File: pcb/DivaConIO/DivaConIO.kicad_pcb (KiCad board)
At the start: 2 copper layers, 55.9 x 70.5 mm, 35 parts, among them J1 DPad Buttons, J10 SWD, J2 Slider i2c, J3 Display i2c, J4 Face Buttons, J5 Button LEDs, J6 L Buttons, J7 Fn Buttons, J8 R Buttons, J9 Slider LEDs, Q1 BC847, Q2 BC847, Q3 BC847, Q4 BC847, SW1 Reset, U1 Pico, U2 SN74LVC1T45DCK

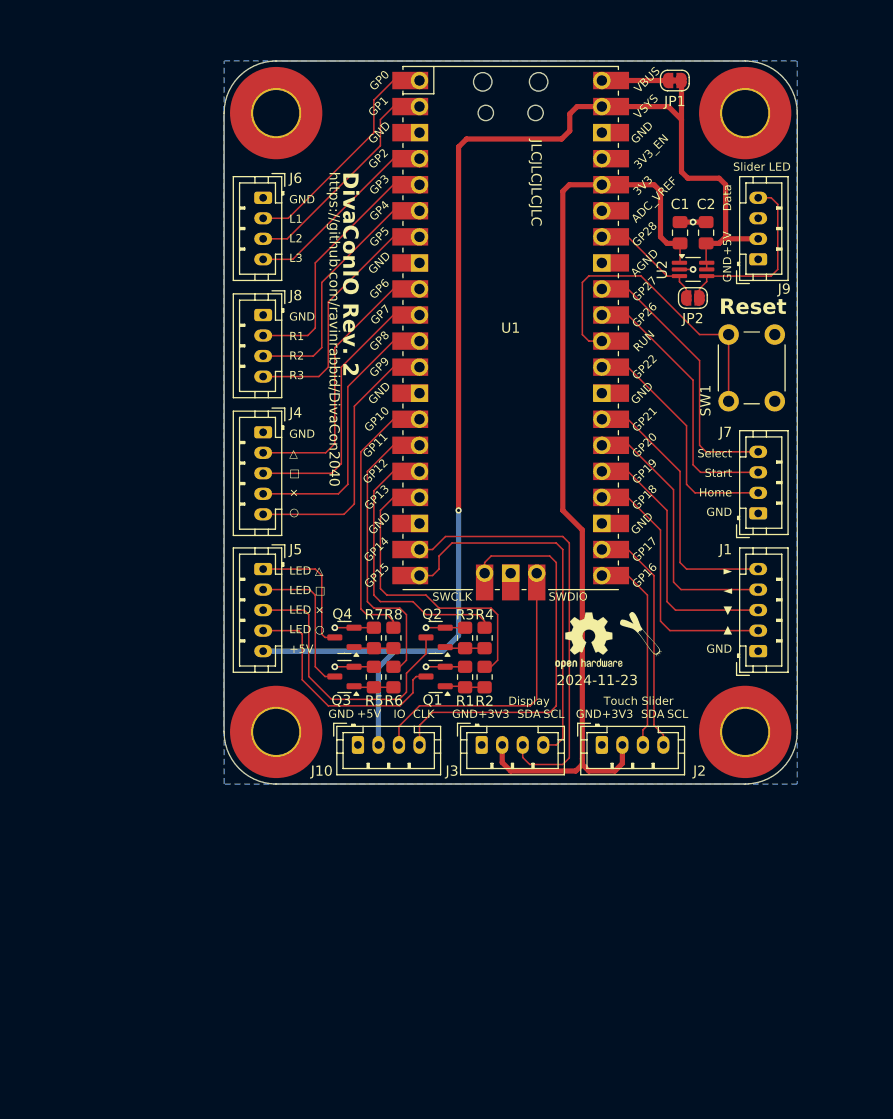
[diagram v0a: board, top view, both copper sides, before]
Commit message: relaid out IO board
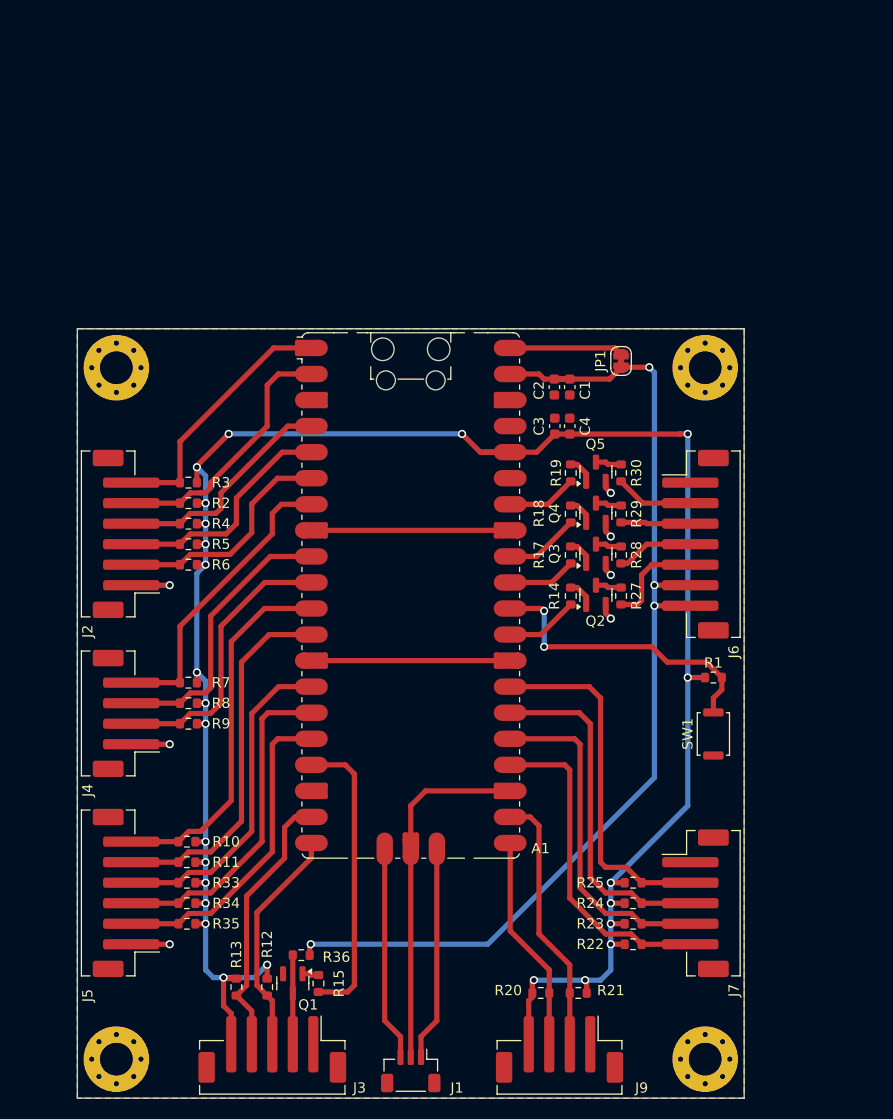
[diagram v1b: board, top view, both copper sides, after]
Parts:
- removed J10: SWD, Connector_JST:JST_PH_B4B-PH-K_1x04_P2.00mm_Vertical
- removed J8: R Buttons, Connector_JST:JST_PH_B4B-PH-K_1x04_P2.00mm_Vertical
- removed JP2: Bridge LED Data, Jumper:SolderJumper-2_P1.3mm_Open_RoundedPad1.0x1.5mm
- removed REF**: OSHW-Logo2_7.3x6mm_SilkScreen, Symbol:OSHW-Logo2_7.3x6mm_SilkScreen
- removed REF**: LOGO, CustomLogos:Leek-Logo_6.3mm_Silkscreen
- removed U1: Pico, DivaConIO:RPi_Pico_SMD_TH
- removed U2: SN74LVC1T45DCK, Package_TO_SOT_SMD:SOT-363_SC-70-6_Handsoldering
- added A1: RaspberryPi_Pico, Module:RaspberryPi_Pico_SMD_HandSolder, F.Cu at (132.5, 101.0)
- added C3: 1u0, Capacitor_SMD:C_0603_1608Metric, F.Cu at (146.5, 84.5)
- added C4: 100n, Capacitor_SMD:C_0603_1608Metric, F.Cu at (148.0, 84.5)
- added Q5: BSS138, Package_TO_SOT_SMD:SOT-23, F.Cu at (150.6, 88.9)
- added R10: 10K, Resistor_SMD:R_0603_1608Metric, F.Cu at (110.7, 125.0)
- added R11: 10K, Resistor_SMD:R_0603_1608Metric, F.Cu at (110.7, 127.0)
- added R12: 4K7, Resistor_SMD:R_0603_1608Metric, F.Cu at (118.5, 139.2)
- added R13: 4K7, Resistor_SMD:R_0603_1608Metric, F.Cu at (115.5, 139.2)
- added R14: 10R, Resistor_SMD:R_0603_1608Metric, F.Cu at (148.1, 101.0)
- added R15: 10R, Resistor_SMD:R_0603_1608Metric, F.Cu at (123.5, 138.8)
- added R17: 10R, Resistor_SMD:R_0603_1608Metric, F.Cu at (148.1, 97.0)
- added R18: 10R, Resistor_SMD:R_0603_1608Metric, F.Cu at (148.1, 93.0)
- added R19: 10R, Resistor_SMD:R_0603_1608Metric, F.Cu at (148.1, 89.0)
- added R20: 4K7, Resistor_SMD:R_0603_1608Metric, F.Cu at (145.2, 139.8)
- added R21: 4K7, Resistor_SMD:R_0603_1608Metric, F.Cu at (148.8, 139.8)
- added R22: 10K, Resistor_SMD:R_0603_1608Metric, F.Cu at (154.2, 135.0)
- added R23: 10K, Resistor_SMD:R_0603_1608Metric, F.Cu at (154.2, 133.0)
- added R24: 10K, Resistor_SMD:R_0603_1608Metric, F.Cu at (154.2, 131.0)
- added R25: 10K, Resistor_SMD:R_0603_1608Metric, F.Cu at (154.2, 129.0)
- added R27: 330R, Resistor_SMD:R_0603_1608Metric, F.Cu at (153.0, 101.0)
- added R28: 330R, Resistor_SMD:R_0603_1608Metric, F.Cu at (153.0, 97.0)
- added R29: 330R, Resistor_SMD:R_0603_1608Metric, F.Cu at (153.0, 93.0)
- added R30: 330R, Resistor_SMD:R_0603_1608Metric, F.Cu at (153.0, 89.0)
- added R33: 10K, Resistor_SMD:R_0603_1608Metric, F.Cu at (110.7, 129.0)
- added R34: 10K, Resistor_SMD:R_0603_1608Metric, F.Cu at (110.7, 131.0)
- added R35: 10K, Resistor_SMD:R_0603_1608Metric, F.Cu at (110.7, 133.0)
- added R36: 4K7, Resistor_SMD:R_0603_1608Metric, F.Cu at (121.8, 136.1)
- added R9: 10K, Resistor_SMD:R_0603_1608Metric, F.Cu at (110.8, 113.5)
- C1: value 0.1uF -> 1u0; footprint Capacitor_SMD:C_0805_2012Metric_Pad1.18x1.45mm_HandSolder -> Capacitor_SMD:C_0603_1608Metric
- C2: value 0.1uF -> 100n; footprint Capacitor_SMD:C_0805_2012Metric_Pad1.18x1.45mm_HandSolder -> Capacitor_SMD:C_0603_1608Metric
- H1, H2, H3, H4: footprint MountingHole:MountingHole_4.5mm_Pad_TopOnly -> MountingHole:MountingHole_3.2mm_M3_Pad_Via
- J1: value DPad Buttons -> JST_SH_BM03B-SRSS-TB; footprint Connector_JST:JST_PH_B5B-PH-K_1x05_P2.00mm_Vertical -> Connector_JST:JST_SH_BM03B-SRSS-TB_1x03-1MP_P1.00mm_Vertical
- J2: value Slider i2c -> Conn_01x06; footprint Connector_JST:JST_PH_B4B-PH-K_1x04_P2.00mm_Vertical -> Connector_JST:JST_PH_B6B-PH-SM4-TB_1x06-1MP_P2.00mm_Vertical
- J3: value Display i2c -> Conn_01x05; footprint Connector_JST:JST_PH_B4B-PH-K_1x04_P2.00mm_Vertical -> Connector_JST:JST_PH_B5B-PH-SM4-TB_1x05-1MP_P2.00mm_Vertical
- J4: value Face Buttons -> Fn Buttons; footprint Connector_JST:JST_PH_B5B-PH-K_1x05_P2.00mm_Vertical -> Connector_JST:JST_PH_B4B-PH-SM4-TB_1x04-1MP_P2.00mm_Vertical
- J5: value Button LEDs -> Conn_01x06; footprint Connector_JST:JST_PH_B5B-PH-K_1x05_P2.00mm_Vertical -> Connector_JST:JST_PH_B6B-PH-SM4-TB_1x06-1MP_P2.00mm_Vertical
- J6: value L Buttons -> Conn_01x07; footprint Connector_JST:JST_PH_B4B-PH-K_1x04_P2.00mm_Vertical -> Connector_JST:JST_PH_B7B-PH-SM4-TB_1x07-1MP_P2.00mm_Vertical
- J7: value Fn Buttons -> Conn_01x05; footprint Connector_JST:JST_PH_B4B-PH-K_1x04_P2.00mm_Vertical -> Connector_JST:JST_PH_B5B-PH-SM4-TB_1x05-1MP_P2.00mm_Vertical
- J9: value Slider LEDs -> Display i2c; footprint Connector_JST:JST_PH_B4B-PH-K_1x04_P2.00mm_Vertical -> Connector_JST:JST_PH_B4B-PH-SM4-TB_1x04-1MP_P2.00mm_Vertical
- JP1: value Bridge VSYS -> SolderJumper_2_Bridged
- Q1, Q2, Q3, Q4: value BC847 -> BSS138
- R1, R2, R3, R4, R5, R6, R7, R8: value 4.7k -> 10K; footprint Resistor_SMD:R_0805_2012Metric_Pad1.20x1.40mm_HandSolder -> Resistor_SMD:R_0603_1608Metric
- SW1: value Reset -> SW_Push; footprint Button_Switch_THT:SW_PUSH_6mm -> Button_Switch_SMD:SW_Push_SPST_NO_Alps_SKRK
- moved H2 110.7 mm to (103.8, 146.2)
- moved J9 79.4 mm to (147.0, 145.2), turned to 180 degrees
- moved J6 54.0 mm to (160.2, 96.0)
- moved J1 53.1 mm to (132.5, 147.3), turned to 180 degrees
- moved J2 50.7 mm to (104.8, 95.0), turned to 90 degrees
- moved H1 48.6 mm to (161.2, 78.8)
- moved H4 38.8 mm to (103.8, 78.8)
- moved J7 38.5 mm to (160.2, 131.0), turned to -90 degrees
- moved J3 36.0 mm to (119.0, 145.2), turned to 180 degrees
- moved R2 34.5 mm to (110.8, 90.0), turned to 180 degrees
- moved J5 34.3 mm to (104.8, 130.0), turned to 90 degrees
- moved Q1 33.0 mm to (121.0, 138.8), turned to -90 degrees
- moved SW1 32.5 mm to (162.0, 114.5)
- moved H3 32.1 mm to (161.2, 146.2)
- moved R4 30.9 mm to (110.8, 94.0), turned to 180 degrees
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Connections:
- C1 pad 1: +3V3 -> +5V
- J1 pad 1: GND -> Net-(A1-SWDIO)
- J1 pad 2: Button Up -> GND
- J1 pad 3: Button Down -> Net-(A1-SWCLK)
- J2 pad 2: +3V3 -> /Button_R1
- J2 pad 3: Slider SDA -> /Button_R2
- J2 pad 4: Slider SCL -> /Button_R3
- J3 pad 2: +3V3 -> Net-(J3-Pin_2)
- J3 pad 3: Display SDA -> /Slider_I2C1_SCL
- J3 pad 4: Display SCL -> /Slider_I2C1_SDA
- J4 pad 2: Button Triangle -> /Button_Home
- J4 pad 3: Button Square -> /Button_Start
- J4 pad 4: Button Cross -> /Button_Select
- J5 pad 1: Net-(J5-Pin_1) -> GND
- J5 pad 2: Net-(J5-Pin_2) -> /Button_L3
- J5 pad 3: Net-(J5-Pin_3) -> /Button_L2
- J5 pad 4: Net-(J5-Pin_4) -> /Button_L1
- J5 pad 5: +5V -> /Button_Up
- J6 pad 2: Button L1 -> /LED_Circle
- J6 pad 3: Button L2 -> /LED_Cross
- J6 pad 4: Button L3 -> /LED_Square
- J7 pad 2: Button Home -> /Button_Circle
- J7 pad 3: Button Start -> /Button_Cross
- J7 pad 4: Button Select -> /Button_Square
- J9 pad 2: +5V -> /Display_I2C0_SCL
- J9 pad 3: unconnected-(J9-Pin_3-Pad3) -> /Display_I2C0_SDA
- J9 pad 4: Net-(J9-Pin_4) -> +3V3
- Q1 pad 1: Net-(Q1-B) -> Net-(Q1-G)
- Q1 pad 3: Net-(J5-Pin_4) -> Net-(J3-Pin_2)
- Q2 pad 1: Net-(Q2-B) -> Net-(Q2-G)
- Q2 pad 3: Net-(J5-Pin_3) -> Net-(Q2-D)
- Q3 pad 1: Net-(Q3-B) -> Net-(Q3-G)
- Q3 pad 3: Net-(J5-Pin_2) -> Net-(Q3-D)
- Q4 pad 1: Net-(Q4-B) -> Net-(Q4-G)
- Q4 pad 3: Net-(J5-Pin_1) -> Net-(Q4-D)
- R1 pad 1: GND -> +3V3
- R1 pad 2: Net-(Q1-B) -> Net-(A1-RUN)
- R2 pad 1: Net-(Q1-B) -> +3V3
- R2 pad 2: LED Circle -> /Button_Left
- R3 pad 1: GND -> +3V3
- R3 pad 2: Net-(Q2-B) -> /Button_Right
- R4 pad 1: Net-(Q2-B) -> +3V3
- R4 pad 2: LED Cross -> /Button_R3
- R5 pad 1: GND -> +3V3
- R5 pad 2: Net-(Q3-B) -> /Button_R2
- R6 pad 1: Net-(Q3-B) -> +3V3
- R6 pad 2: LED Square -> /Button_R1
- R7 pad 1: GND -> +3V3
- R7 pad 2: Net-(Q4-B) -> /Button_Select
- R8 pad 1: Net-(Q4-B) -> +3V3
- R8 pad 2: LED Triangle -> /Button_Start
- SW1 pad 1: Net-(U1-RUN) -> GND
- SW1 pad 2: GND -> Net-(A1-RUN)
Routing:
- net +3V3: track 91.7 -> 210.4 mm, vias 0 -> 25
- net GND: track 19.1 -> 90.6 mm, vias 6 -> 7
- net Display SDA: track 42.7 -> 0.00 mm
- net SWCLK: track 38.6 -> 0.00 mm
- net Display SCL: track 36.9 -> 0.00 mm
- net /Button_Down: track 0.00 -> 36.1 mm
- net /Button_Up: track 0.00 -> 35.8 mm
- net /Button_Circle: track 0.00 -> 34.8 mm
- net /Button_Cross: track 0.00 -> 34.0 mm
- net /Button_Square: track 0.00 -> 33.2 mm
- net Net-(U1-RUN): track 33.2 -> 0.00 mm
- net /Button_L2: track 0.00 -> 32.3 mm
- net /Button_L1: track 0.00 -> 32.2 mm
- net /Button_Triangle: track 0.00 -> 32.1 mm
- net /Button_L3: track 0.00 -> 31.2 mm
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- added copper zone on F.Cu, net GND
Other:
- board size 55.9 x 70.5 mm -> 65 x 75 mm
- board text removed: "${ISSUE_DATE}"
- board text removed: "${TITLE} Rev. ${REVISION}"
- board text removed: "+3V3"
- board text removed: "+5V"
- board text removed: "CLK"
- board text removed: "Data"
- board text removed: "Display"
- board text removed: "GND"
- board text removed: "Home"
- board text removed: "IO"
- board text removed: "JLCJLCJLCJLC"
- board text removed: "L1"
- board text removed: "L2"
- board text removed: "L3"
- board text removed: "LED ×"
- board text removed: "LED □"
- board text removed: "LED △"
- board text removed: "LED ○"
- board text removed: "R1"
- board text removed: "R2"
- board text removed: "R3"
- board text removed: "Reset"
- board text removed: "SCL"
- board text removed: "SDA"
- board text removed: "Select"
- board text removed: "Slider LED"
- board text removed: "Start"
- board text removed: "Touch Slider"
- board text removed: "https://github.com/ravinrabbid/DivaCon2040"
- board text removed: "×"
- board text removed: "□"
- board text removed: "▲"
- board text removed: "△"
- board text removed: "►"
- board text removed: "▼"
- board text removed: "◄"
- board text removed: "○"

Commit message: documenting wiring diagram
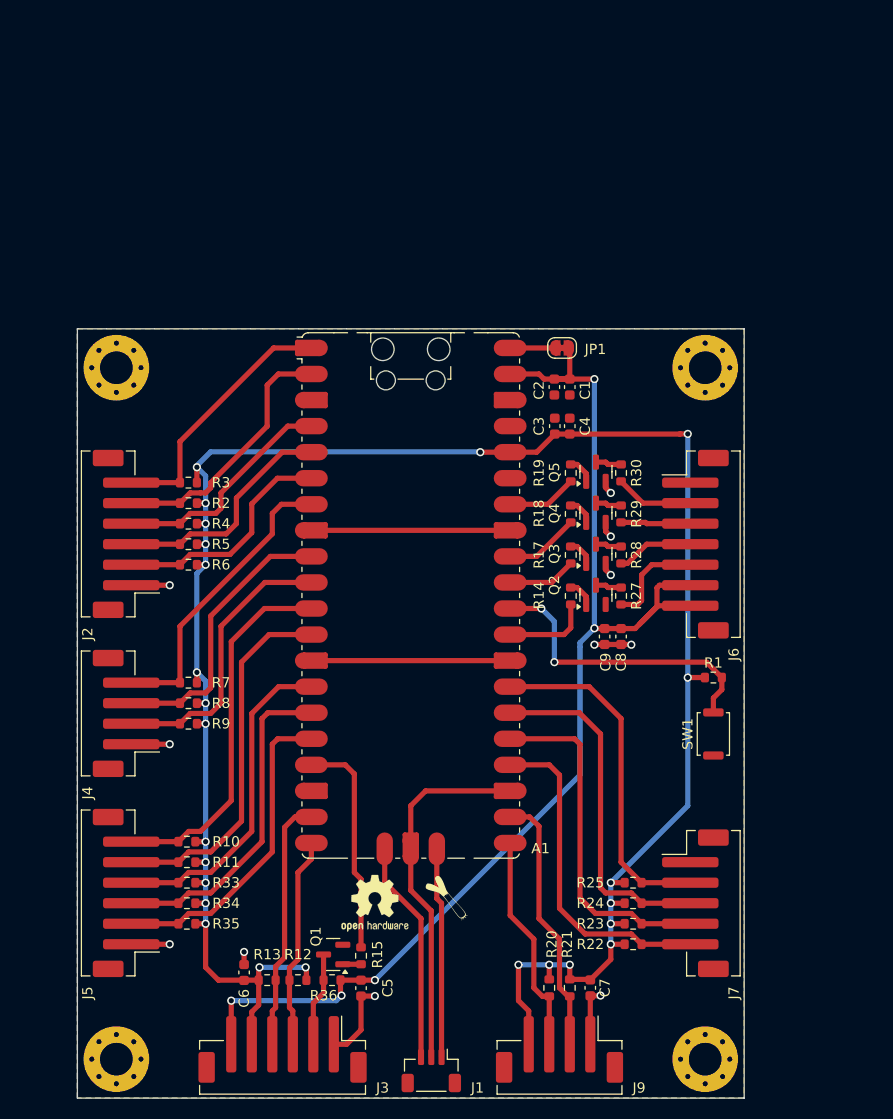
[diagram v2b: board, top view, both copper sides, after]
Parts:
- added C5: 1u0, Capacitor_SMD:C_0603_1608Metric, F.Cu at (127.7, 139.3)
- added C6: 1u0, Capacitor_SMD:C_0603_1608Metric, F.Cu at (116.2, 137.8)
- added C7: 1u0, Capacitor_SMD:C_0603_1608Metric, F.Cu at (150.0, 139.2)
- added C8: 1u0, Capacitor_SMD:C_0603_1608Metric, F.Cu at (153.0, 105.0)
- added C9: 1u0, Capacitor_SMD:C_0603_1608Metric, F.Cu at (151.4, 105.0)
- added SYM1: Leek, CustomLogos:Leek-Logo_6.3mm_Silkscreen, F.Cu at (136.0, 130.5)
- added SYM2: Logo_Open_Hardware_Small, Symbol:OSHW-Logo2_7.3x6mm_SilkScreen, F.Cu at (129.0, 131.0)
- J3: value Conn_01x05 -> Conn_01x06; footprint Connector_JST:JST_PH_B5B-PH-SM4-TB_1x05-1MP_P2.00mm_Vertical -> Connector_JST:JST_PH_B6B-PH-SM4-TB_1x06-1MP_P2.00mm_Vertical
- J6: value Conn_01x07 -> Conn_01x07_MountingPin
- J7: value Conn_01x05 -> Conn_01x05_MountingPin
- J9: value Display i2c -> Conn_01x04_MountingPin
- moved JP1 5.89 mm to (147.2, 76.9), turned to 180 degrees
- moved R15 4.95 mm to (127.7, 136.1), turned to -90 degrees
- moved Q1 4.84 mm to (124.9, 136.0), turned to 180 degrees
- moved R36 3.87 mm to (124.8, 138.5)
- moved R12 3.08 mm to (121.5, 138.5), turned to 180 degrees
- moved R13 3.08 mm to (118.5, 138.5), turned to 0 degrees
- moved J1 2.00 mm to (134.5, 147.3)
- moved J3 1.00 mm to (120.0, 145.2)
- moved R20 0.96 mm to (146.0, 139.2), turned to -90 degrees
- moved R21 0.96 mm to (148.0, 139.2), turned to -90 degrees
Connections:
- J1 pad MP: (no net) -> GND
- J2 pad MP: (no net) -> GND
- J3 pad MP: (no net) -> GND
- J4 pad MP: (no net) -> GND
- J5 pad MP: (no net) -> GND
- J6 pad MP: (no net) -> GND
- J7 pad MP: (no net) -> GND
- J9 pad MP: (no net) -> GND
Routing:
- net GND: track 90.6 -> 108.3 mm, vias 7 -> 11
- net +5V: track 104.3 -> 120.6 mm, vias 4 -> 5
- net /Slider_LED_Data: track 28.9 -> 21.7 mm
- net Net-(A1-VBUS): track 11.1 -> 4.41 mm
- net +3V3: track 210.4 -> 213.5 mm
- net /Slider_I2C1_SDA: track 26.7 -> 24.7 mm
- net /Slider_I2C1_SCL: track 22.4 -> 20.6 mm
- net /LED_En_Triangle: track 7.13 -> 8.46 mm
- net /Button_Circle: track 34.8 -> 33.7 mm
- net Net-(A1-SWCLK): track 21.7 -> 22.6 mm
- net /Button_Square: track 33.2 -> 33.8 mm

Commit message: placing both I2C buses on the same connector
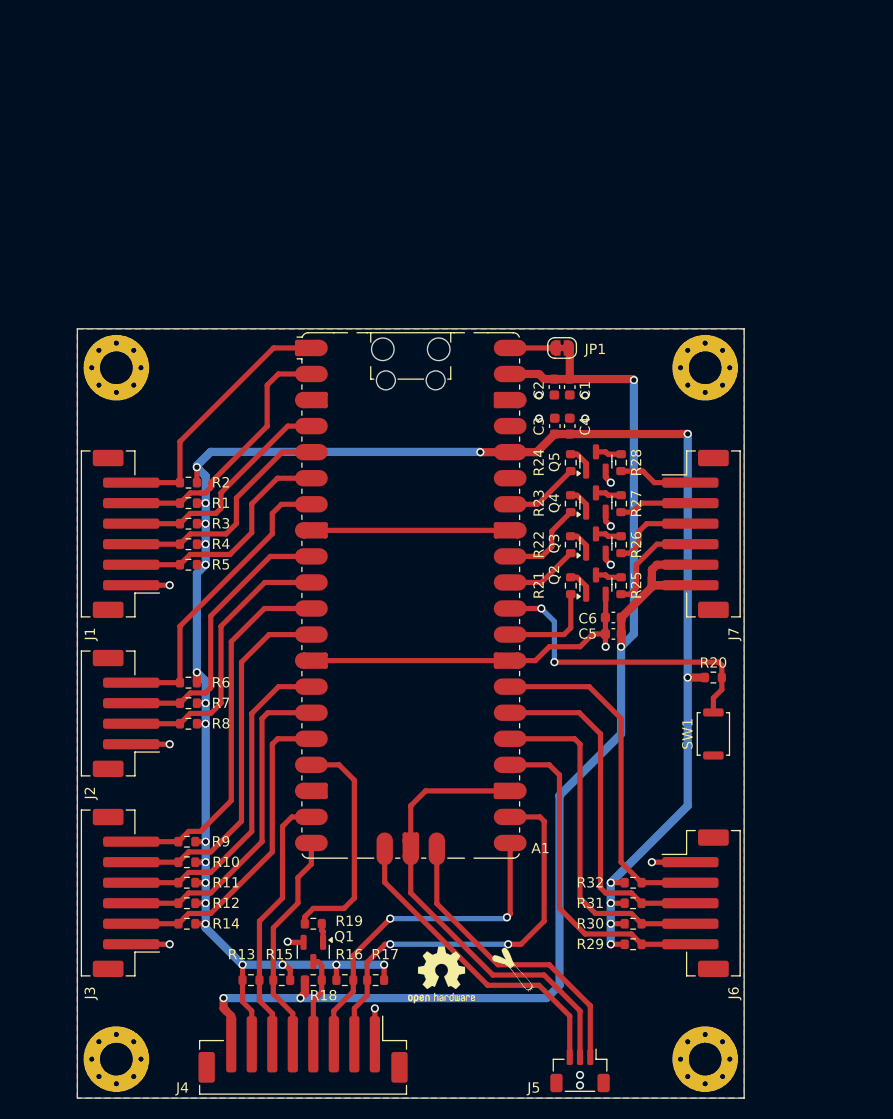
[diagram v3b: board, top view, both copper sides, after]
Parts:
- removed the C5 at (127.7, 139.3)
- removed the C6 at (116.2, 137.8)
- removed C7: 1u0, Capacitor_SMD:C_0603_1608Metric
- removed J9: Conn_01x04_MountingPin, Connector_JST:JST_PH_B4B-PH-SM4-TB_1x04-1MP_P2.00mm_Vertical
- removed the R20 at (146.0, 139.2)
- removed the R21 at (148.0, 139.2)
- added R16: 4K7, Resistor_SMD:R_0603_1608Metric, F.Cu at (126.1, 138.5)
- added R17: 4K7, Resistor_SMD:R_0603_1608Metric, F.Cu at (129.1, 138.5)
- J1: renamed from J2; value Conn_01x06 -> Conn_01x06_MountingPin
- J2: renamed from J7; value Conn_01x05_MountingPin -> Conn_01x04_MountingPin; footprint Connector_JST:JST_PH_B5B-PH-SM4-TB_1x05-1MP_P2.00mm_Vertical -> Connector_JST:JST_PH_B4B-PH-SM4-TB_1x04-1MP_P2.00mm_Vertical
- J3: value Conn_01x06 -> Conn_01x06_MountingPin
- J4: value Fn Buttons -> Conn_01x08_MountingPin; footprint Connector_JST:JST_PH_B4B-PH-SM4-TB_1x04-1MP_P2.00mm_Vertical -> Connector_JST:JST_PH_B8B-PH-SM4-TB_1x08-1MP_P2.00mm_Vertical
- J6: value Conn_01x07_MountingPin -> Conn_01x05_MountingPin; footprint Connector_JST:JST_PH_B7B-PH-SM4-TB_1x07-1MP_P2.00mm_Vertical -> Connector_JST:JST_PH_B5B-PH-SM4-TB_1x05-1MP_P2.00mm_Vertical
- J7: renamed from J5; value Conn_01x06 -> Conn_01x06_MountingPin
- moved J7 65.6 mm to (160.2, 95.0), turned to -90 degrees
- moved J2 58.5 mm to (104.8, 112.5), turned to 90 degrees
- moved J4 37.0 mm to (122.0, 145.2), turned to 180 degrees
- moved J6 35.0 mm to (160.2, 131.0)
- moved J3 21.6 mm to (104.8, 130.0), turned to 90 degrees
- moved J5 14.5 mm to (149.0, 147.3)
- moved SYM1 9.55 mm to (142.5, 137.5)
- moved SYM2 9.55 mm to (135.5, 138.0)
- moved R19 5.60 mm to (123.0, 133.0), turned to 0 degrees
- moved R13 4.58 mm to (116.9, 138.5), turned to 0 degrees
- moved C6 2.04 mm to (152.2, 103.2), turned to 180 degrees
- moved Q1 1.95 mm to (123.0, 135.8), turned to -90 degrees
- moved R18 1.83 mm to (123.0, 138.5), turned to 0 degrees
- moved R15 1.42 mm to (119.9, 138.5), turned to 180 degrees
- moved Q2 1.00 mm to (150.6, 99.9)
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- renumbered C8 to C5, C9 to C6, J1 to J5, R2 to R1, R11 to R10, R33 to R11, R34 to R12, R12 to R13, R35 to R14, R13 to R15, R36 to R18, R15 to R19, R3 to R2, R1 to R20, R14 to R21, R17 to R22, R18 to R23, R19 to R24, R27 to R25, R28 to R26, R29 to R27, R30 to R28, R22 to R29, R4 to R3, R23 to R30, R24 to R31, R25 to R32, R5 to R4, R6 to R5, R7 to R6, R8 to R7, R9 to R8, R10 to R9
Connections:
- J2 pad 2: /Button_Circle -> /Button_Home
- J2 pad 3: /Button_Cross -> /Button_Start
- J2 pad 4: /Button_Square -> /Button_Select
- J3 pad 2: Net-(J3-Pin_2) -> /Button_L3
- J3 pad 3: /Slider_I2C1_SCL -> /Button_L2
- J3 pad 4: /Slider_I2C1_SDA -> /Button_L1
- J3 pad 5: +3V3 -> /Button_Up
- J3 pad 6: +5V -> /Button_Down
- J4 pad 2: /Button_Home -> /Display_I2C0_SCL
- J4 pad 3: /Button_Start -> /Display_I2C0_SDA
- J4 pad 4: /Button_Select -> Net-(J4-Pin_4)
- J6 pad 2: /LED_Circle -> /Button_Circle
- J6 pad 3: /LED_Cross -> /Button_Cross
- J6 pad 4: /LED_Square -> /Button_Square
- J6 pad 5: /LED_Triangle -> /Button_Triangle
- J7 pad 1: GND -> /LED_Circle
- J7 pad 2: /Button_L3 -> /LED_Cross
- J7 pad 3: /Button_L2 -> /LED_Square
- J7 pad 4: /Button_L1 -> /LED_Triangle
- J7 pad 5: /Button_Up -> +5V
- J7 pad 6: /Button_Down -> +5V
- Q1 pad 3: Net-(J3-Pin_2) -> Net-(J4-Pin_4)
- R13 pad 2: /Slider_I2C1_SCL -> /Slider_I2C1_SDA
- R15 pad 2: /Slider_I2C1_SDA -> /Slider_I2C1_SCL
- R18 pad 2: Net-(J3-Pin_2) -> Net-(J4-Pin_4)
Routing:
- net +5V: track 120.6 -> 139.6 mm, vias 5 -> 4
- net GND: track 108.3 -> 123.4 mm, vias 11 -> 16
- net /Display_I2C0_SCL: track 25.8 -> 40.7 mm, vias 0 -> 2
- net +3V3: track 213.5 -> 199.6 mm, vias 25 -> 24
- net /Display_I2C0_SDA: track 21.6 -> 33.3 mm, vias 0 -> 2
- net Net-(J3-Pin_2): track 9.16 -> 0.00 mm
- net Net-(J4-Pin_4): track 0.00 -> 9.00 mm
- net Net-(A1-SWDIO): track 21.3 -> 30.2 mm
- net Net-(A1-SWCLK): track 22.6 -> 31.5 mm
- net /LED_En_Cross: track 7.28 -> 8.59 mm
- net /Slider_I2C1_SCL: track 20.6 -> 21.9 mm
- net /Slider_I2C1_SDA: track 24.7 -> 25.9 mm
- net /LED_Square: track 7.53 -> 8.67 mm
- net /LED_En_Triangle: track 8.46 -> 9.46 mm
- net /Slider_LED_Data: track 21.7 -> 22.6 mm
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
